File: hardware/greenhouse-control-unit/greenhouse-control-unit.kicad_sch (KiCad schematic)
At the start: 51 parts, among them J1 Buck_Conn_01x01_Female, J10 Conn_01x08, J11 Conn_01x08, J12 Conn_01x05_Female, J15 Conn_01x05_Female, J16 Conn_01x05_Female, J2 Buck_Conn_01x01_Female, J3 Buck_Conn_01x01_Female, J4 Buck_Conn_01x01_Female, J5 Molex_KK-396_01x02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

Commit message: Remove LEDs from PSU/batt d/c
Sharing IO pin causing gate/base to be pulled high and/or LED to be partially on
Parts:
- removed D2, D6: LED, LED_THT:LED_D5.0mm, symbol Device:LED
- removed Q4: BC337, Package_TO_SOT_THT:TO-92_Inline, symbol Transistor_BJT:BC337
- removed R1, R17: 2k, Resistor_THT:R_Axial_DIN0207_L6.3mm_D2.5mm_P7.62mm_Horizontal, symbol Device:R_US
- removed R16: 10k, Resistor_THT:R_Axial_DIN0207_L6.3mm_D2.5mm_P7.62mm_Horizontal, symbol Device:R_US
- Q6: Field4 Note: Flipped -> Note: Upside down
- R11: value 10k -> 1k
- R15: value 10k -> 2k
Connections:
- net SR_Batt_EN is gone; now on net IO_Batt_EN: U1.4 (P0)
- net IO_Batt_EN: now reaches Q6.1 (G), R18.1
- net SR_BatteryLed renamed IO_BatteryLed
- net SR_Beep renamed IO_Beep
- net SR_CaseFan_EN renamed IO_CaseFan_EN
- net SR_PsuLed renamed IO_PsuLed
- net SR_PsuRelay_EN renamed IO_PsuRelay_EN
- no-connect marks 0 -> 13
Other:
- note added: "Case fan draws 200mA; NPN base is 2.5mA."
- note added: "PSU 10V NC relay module is active HIGH. Relay module coil must be open at power on. IO is HIGH at power on. NPN required to drive relay module; Relay module IN requires only 1.7mA, but IO is a weak current source (best used as current sink). Active LOW must be pulled high to 10V to disable. Active HIGH can be pulled high to only 5V to enable."
- note added: "Potential design flaw: IO can only pull battery FET low when PSU is connected, otherwise, FET gate will float, which turns battery half-on. A firmware bug may cause the FET to overheat if the PSU and battery are turned off at the same time."
- note removed: "PSU NC relay module coil must be off at power on; relay module IN is active HIGH, but IO is HIGH at power on."
- moved on the sheet: D3, D4, D5, J1, J2, J3, J4, J5, J6, J7, Q2, Q6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

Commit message: Add a bunch of BJTs
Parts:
- removed D12: LED, LED_THT:LED_D5.0mm, symbol Device:LED
- removed Q1: BC337, Package_TO_SOT_THT:TO-92_Inline, symbol Transistor_BJT:BC337
- removed R15: 2k, Resistor_THT:R_Axial_DIN0207_L6.3mm_D2.5mm_P7.62mm_Horizontal, symbol Device:R_US
- added D6: LED, LED_THT:LED_D5.0mm, symbol Device:LED
- added J13: Beep_Jumper, Connector_PinHeader_2.54mm:PinHeader_1x03_P2.54mm_Vertical, symbol Connector:Conn_01x03_Female
- added Q1: BC557, Package_TO_SOT_THT:TO-92_Inline, symbol Transistor_BJT:BC557
- added Q4, Q5, Q7, Q8: BC337, Package_TO_SOT_THT:TO-92_Inline, symbol Transistor_BJT:BC337
- added R1: 100k, Resistor_THT:R_Axial_DIN0207_L6.3mm_D2.5mm_P7.62mm_Horizontal, symbol Device:R_US
- added R16, R19: 1k, Resistor_THT:R_Axial_DIN0207_L6.3mm_D2.5mm_P7.62mm_Horizontal, symbol Device:R_US
- added R17, R20: 2k, Resistor_THT:R_Axial_DIN0207_L6.3mm_D2.5mm_P7.62mm_Horizontal, symbol Device:R_US
- BZ1: value Buzzer -> 10mA beep
- R13: value 2k -> 1k
- R18: footprint Resistor_THT:R_Axial_DIN0204_L3.6mm_D1.6mm_P5.08mm_Horizontal -> Resistor_THT:R_Axial_DIN0207_L6.3mm_D2.5mm_P7.62mm_Horizontal
- R2: value 10k -> 2k
- R4: value 220R -> 100R
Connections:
- net +10V: now also R18.1, R16.1
- net +3V3: now also R19.1
- net +5V: now also R20.1
- net Batt_GND: no longer R18.2
- net CaseFan_Sink: now also D6.1 (K), Q8.1 (C); no longer Q3.1 (C)
- net GND: now also Q1.1 (C), Q4.3 (E), Q5.3 (E), Q7.3 (E), Q8.3 (E)
- net IO_Batt_EN: now also R1.1; no longer Q6.1 (G), R18.1
- net IO_Beep: now also U1.6 (P2); no longer U1.7 (P3)
- net IO_CaseFan_EN: now also U1.7 (P3), R17.1; no longer U1.5 (P1)
- net IO_PsuRelay_EN: now also U1.5 (P1); no longer U1.6 (P2)
- net at R2.2: now also Q3.2 (B)
- net at R13.2: now also Q3.1 (C), Q7.2 (B)
- net at BZ1.2 (+), D1.1 (K): now also Q7.1 (C)
- net at R4.2: now also J13.1 (Pin_1); no longer BZ1.1 (-)
- new net: Q1.3 (E), Q8.2 (B), R19.2
- new net: Q4.1 (C), Q5.2 (B), R16.2
- new net: Q4.2 (B), R1.2
- new net: Q1.2 (B), R17.2
- new net: D6.2 (A), R20.2
- new net: Q5.1 (C), Q6.1 (G), R18.2
- new net: BZ1.1 (-), J13.2 (Pin_2)
- no-connect marks 13 -> 14
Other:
- note added: "170mA"
- note added: "2mA"
- note added: "8uA"
- note added: "Active HIGH"
- note added: "Active LOW"
- note added: "Case fan draws 200mA nominal."
- note added: "Design flaw/limitation: A firmware bug or IO hardware failure could cause the FET to overheat (i.e. when the PSU and battery are turned off at the same time). Pre IO init, the outputs float. Test confirms: with a 2A load and 2.5V at the gate (both IO pins LOW), the FET will reach 80°C in it's partially on state. Idea: Perhaps a NAND gate could be useful to reset the MCU?"
- note added: "LOW to d/c PSU"
- note added: "LOW to d/c battery"
- note added: "Only works if external 5V power source for micro?!"
- note added: "PSU 10V NC relay module is active HIGH. Relay module coil must be open at power on. IO is HIGH at power on. NPN required to drive relay module; relay module IN requires only 1.7mA, but IO is a weak current source (best used as current sink). Active LOW must be pulled high to 10V to disable. Active HIGH can be pulled high to only 5V to enable."
- note added: "TODO: Connect to battery GND to prevent PSU off while no battery connected? i.e. Only allow battery to power the PSU relay d/c"
- note added: "TODO: R17 redundant?"
- note added: "TODO: Reduce from 500mA NPN's to 100mA"
- note removed: "Case fan draws 200mA; NPN base is 2.5mA."
- note removed: "PSU 10V NC relay module is active HIGH. Relay module coil must be open at power on. IO is HIGH at power on. NPN required to drive relay module; Relay module IN requires only 1.7mA, but IO is a weak current source (best used as current sink). Active LOW must be pulled high to 10V to disable. Active HIGH can be pulled high to only 5V to enable."
- note removed: "Potential design flaw: IO can only pull battery FET low when PSU is connected, otherwise, FET gate will float, which turns battery half-on. A firmware bug may cause the FET to overheat if the PSU and battery are turned off at the same time."
- moved on the sheet: BZ1, D1, D3, D5, Q2, Q6, R10, R11, R18, R3, R4, R7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

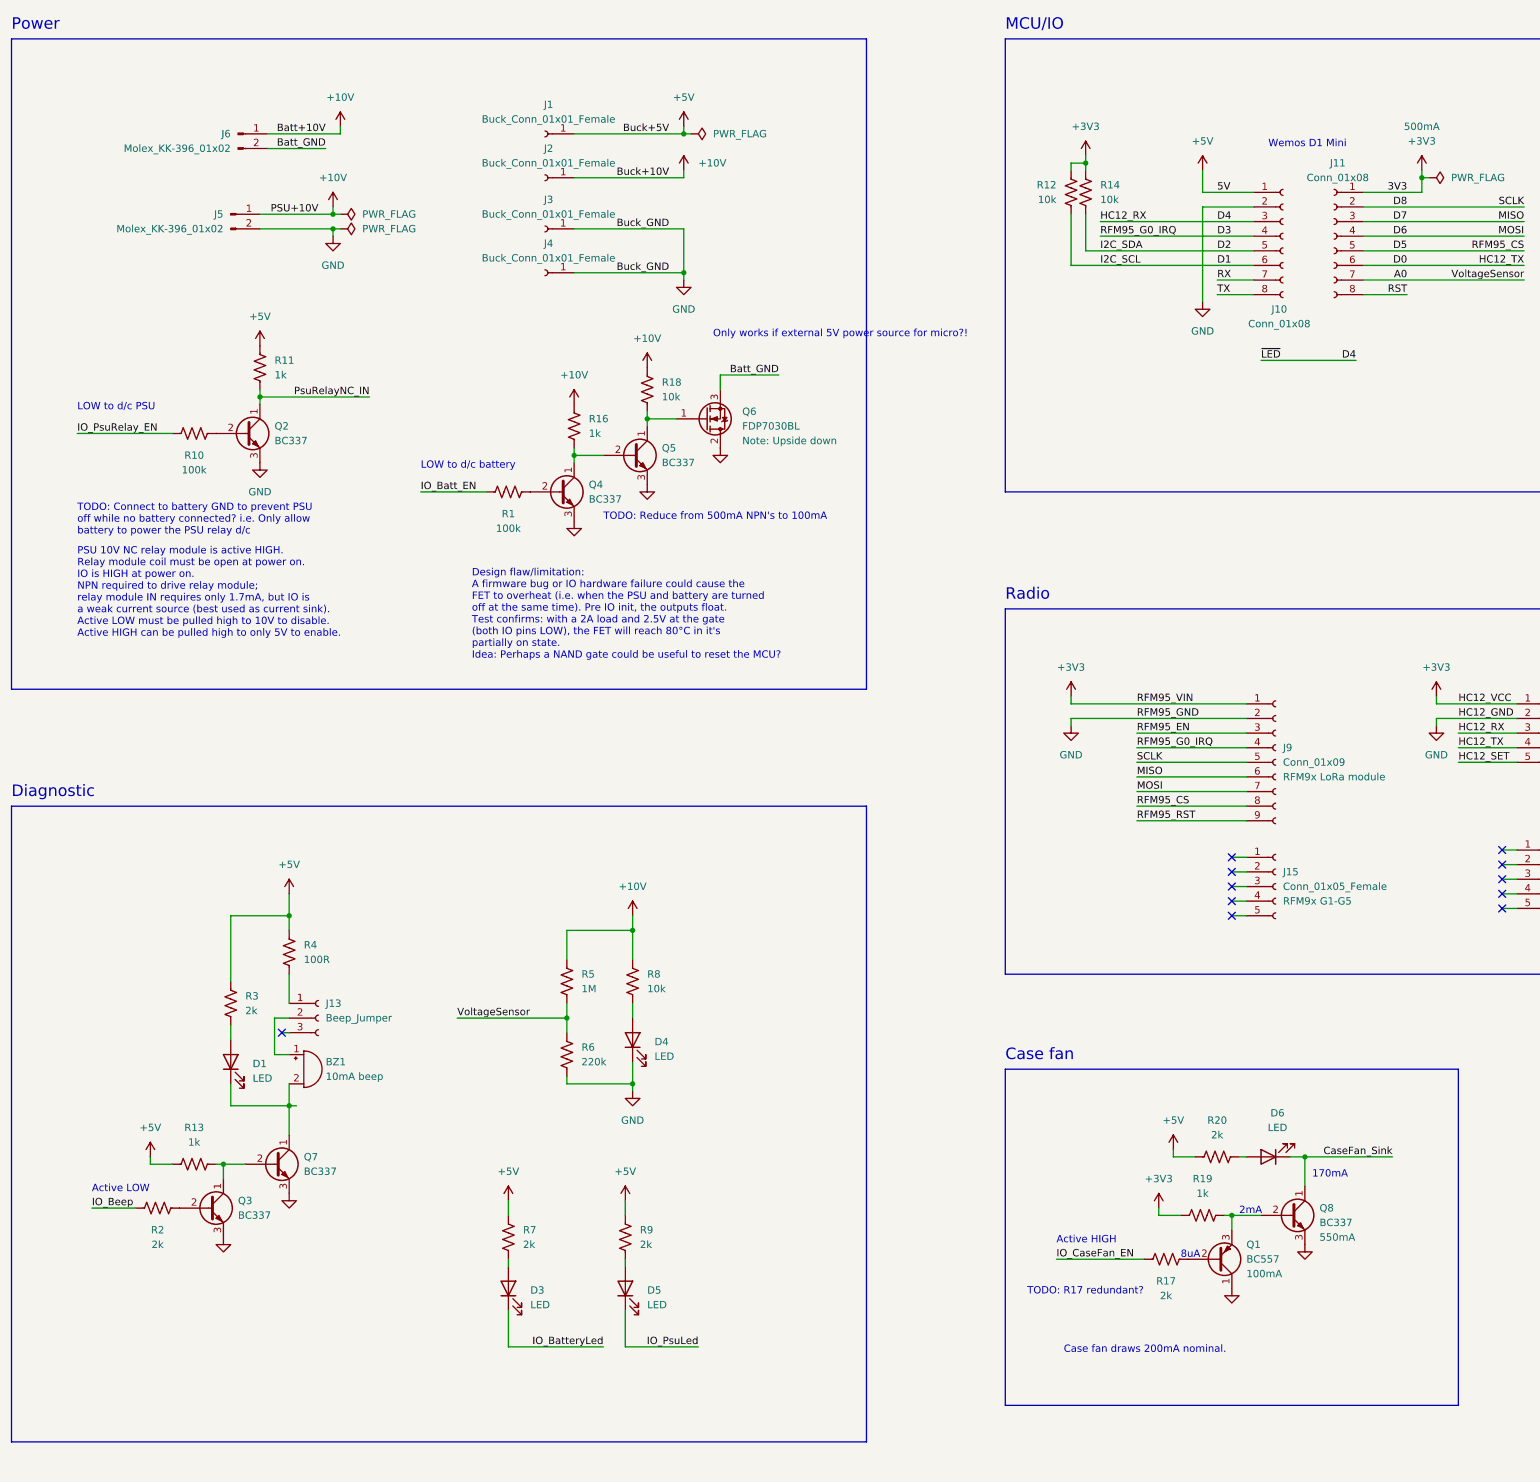
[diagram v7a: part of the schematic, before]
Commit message: Overhauled transistors
PSU, battery, beep, fan
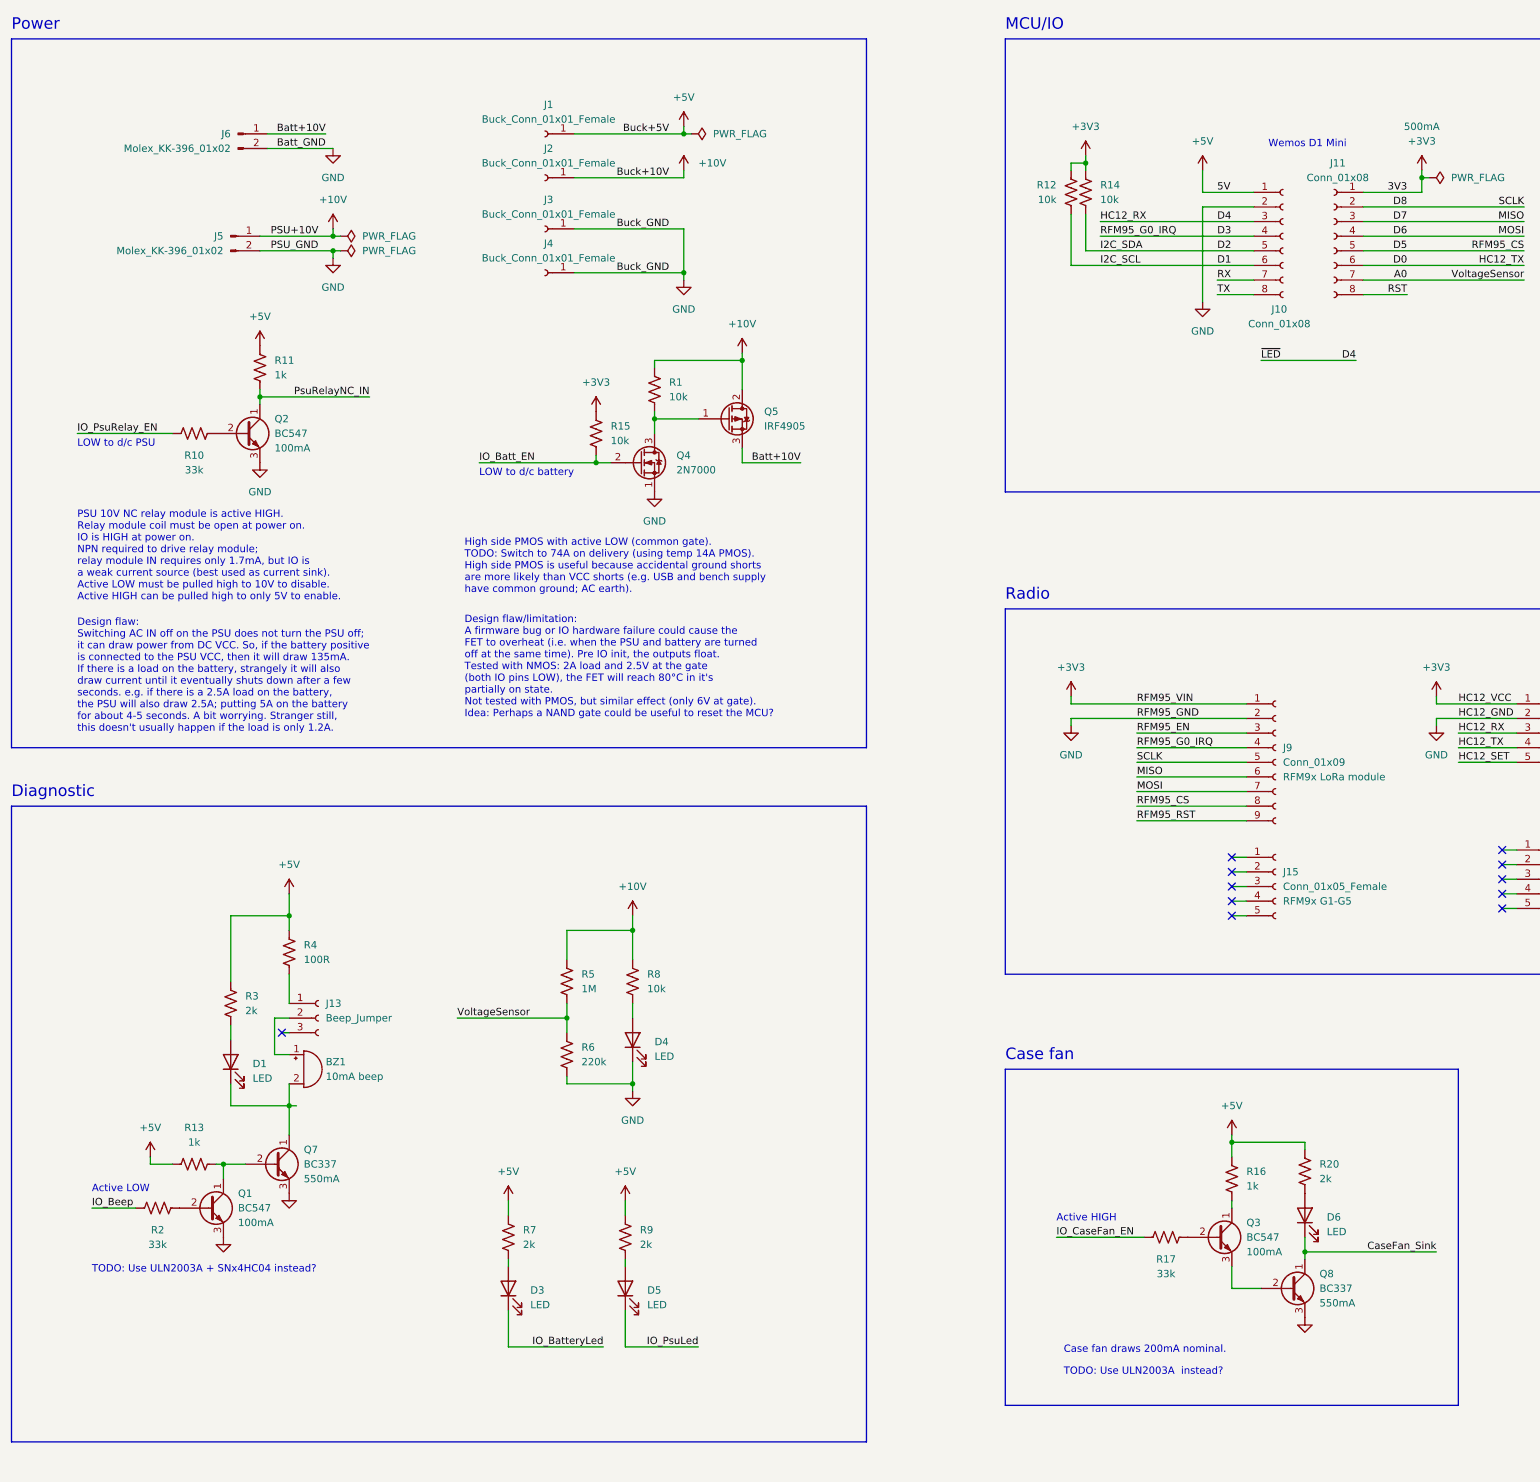
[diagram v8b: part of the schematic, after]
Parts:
- removed Q1: BC557, Package_TO_SOT_THT:TO-92_Inline, symbol Transistor_BJT:BC557
- removed Q2, Q3, Q4, Q5: BC337, Package_TO_SOT_THT:TO-92_Inline, symbol Transistor_BJT:BC337
- removed Q6: FDP7030BL, Package_TO_SOT_THT:TO-220-3_Horizontal_TabDown, symbol Device:Q_NMOS_GDS
- removed R18: 10k, Resistor_THT:R_Axial_DIN0207_L6.3mm_D2.5mm_P7.62mm_Horizontal, symbol Device:R_US
- removed R19: 1k, Resistor_THT:R_Axial_DIN0207_L6.3mm_D2.5mm_P7.62mm_Horizontal, symbol Device:R_US
- added Q1, Q2, Q3: BC547, Package_TO_SOT_THT:TO-92_Inline, symbol Transistor_BJT:BC547
- added Q4: 2N7000, Package_TO_SOT_THT:TO-92_Inline, symbol Transistor_FET:2N7000
- added Q5: IRF4905, Package_TO_SOT_THT:TO-220-3_Horizontal_TabDown, symbol Transistor_FET:IRF4905
- added R15: 10k, Resistor_THT:R_Axial_DIN0207_L6.3mm_D2.5mm_P7.62mm_Horizontal, symbol Device:R_US
- Q7: Ic (none) -> 550mA
- R1: value 100k -> 10k
- R10: value 100k -> 33k
- R17, R2: value 2k -> 33k
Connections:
- net Batt_GND is gone; now on net GND: J6.2 (Pin_2)
- net +10V: now also R1.1, Q5.2 (D); no longer J6.1 (Pin_1), R16.1
- net +3V3: now also R15.1
- net +5V: now also R16.2
- net GND: now also Q1.3 (E), Q2.3 (E), Q4.1 (S)
- net IO_Batt_EN: now also Q4.2 (G), R15.2; no longer R1.1
- net PsuRelayNC_IN: now also Q2.1 (C)
- net at Q8.2 (B): now also Q3.3 (E)
- net at R1.2: now also Q4.3 (D), Q5.1 (G)
- net at R17.2: now also Q3.2 (B)
- net at R10.2: now also Q2.2 (B)
- net at Q7.2 (B), R13.2: now also Q1.1 (C)
- net at R2.2: now also Q1.2 (B)
- new net: Q3.1 (C), R16.1
- new net Batt+10V: J6.1 (Pin_1), Q5.3 (S)
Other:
- note added: "Design flaw/limitation: A firmware bug or IO hardware failure could cause the FET to overheat (i.e. when the PSU and battery are turned off at the same time). Pre IO init, the outputs float. Tested with NMOS: 2A load and 2.5V at the gate (both IO pins LOW), the FET will reach 80°C in it's partially on state. Not tested with PMOS, but similar effect (only 6V at gate). Idea: Perhaps a NAND gate cou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"
- note added: "Design flaw: Switching AC IN off on the PSU does not turn the PSU off; it can draw power from DC VCC. So, if the battery positive is connected to the PSU VCC, then it will draw 135mA. If there is a load on the battery, strangely it will also draw current until it eventually shuts down after a few seconds. e.g. if there is a 2.5A load on the battery, the PSU will also draw 2.5A; putting 5A on the 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"
- note added: "High side PMOS with active LOW (common gate). TODO: Switch to 74A on delivery (using temp 14A PMOS). High side PMOS is useful because accidental ground shorts are more likely than VCC shorts (e.g. USB and bench supply have common ground; AC earth)."
- note added: "TODO: Use ULN2003A + SNx4HC04 instead?"
- note added: "TODO: Use ULN2003A instead?"
- note removed: "170mA"
- note removed: "2mA"
- note removed: "8uA"
- note removed: "Design flaw/limitation: A firmware bug or IO hardware failure could cause the FET to overheat (i.e. when the PSU and battery are turned off at the same time). Pre IO init, the outputs float. Test confirms: with a 2A load and 2.5V at the gate (both IO pins LOW), the FET will reach 80°C in it's partially on state. Idea: Perhaps a NAND gate could be useful to reset the MCU?"
- note removed: "Only works if external 5V power source for micro?!"
- note removed: "TODO: Connect to battery GND to prevent PSU off while no battery connected? i.e. Only allow battery to power the PSU relay d/c"
- note removed: "TODO: R17 redundant?"
- note removed: "TODO: Reduce from 500mA NPN's to 100mA"
- moved on the sheet: D6, J5, Q8, R17, R20
